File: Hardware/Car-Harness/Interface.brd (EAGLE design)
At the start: 99.6 x 99.8 mm, 56 parts, among them J1 34912-8020, J2 34912-8020, J4 632722110112, J5 OBDII-FEMALEFEMALE, Q1 6.5A/20V/35mΩ, Q2 5.8A/30V/35mΩ, Q3 6.5A/20V/35mΩ, Q4 5.8A/30V/35mΩ

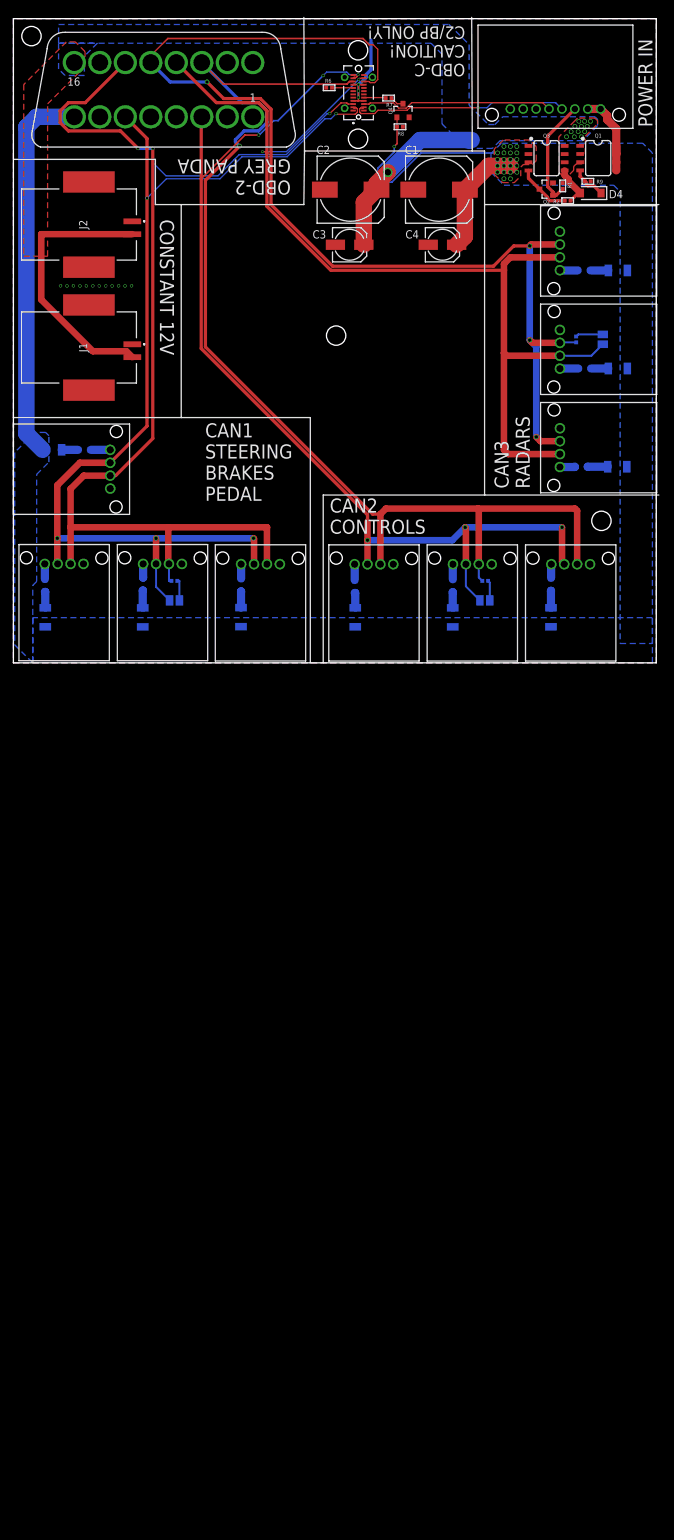
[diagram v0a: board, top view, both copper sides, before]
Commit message: ibooster v2, stm32teensy work
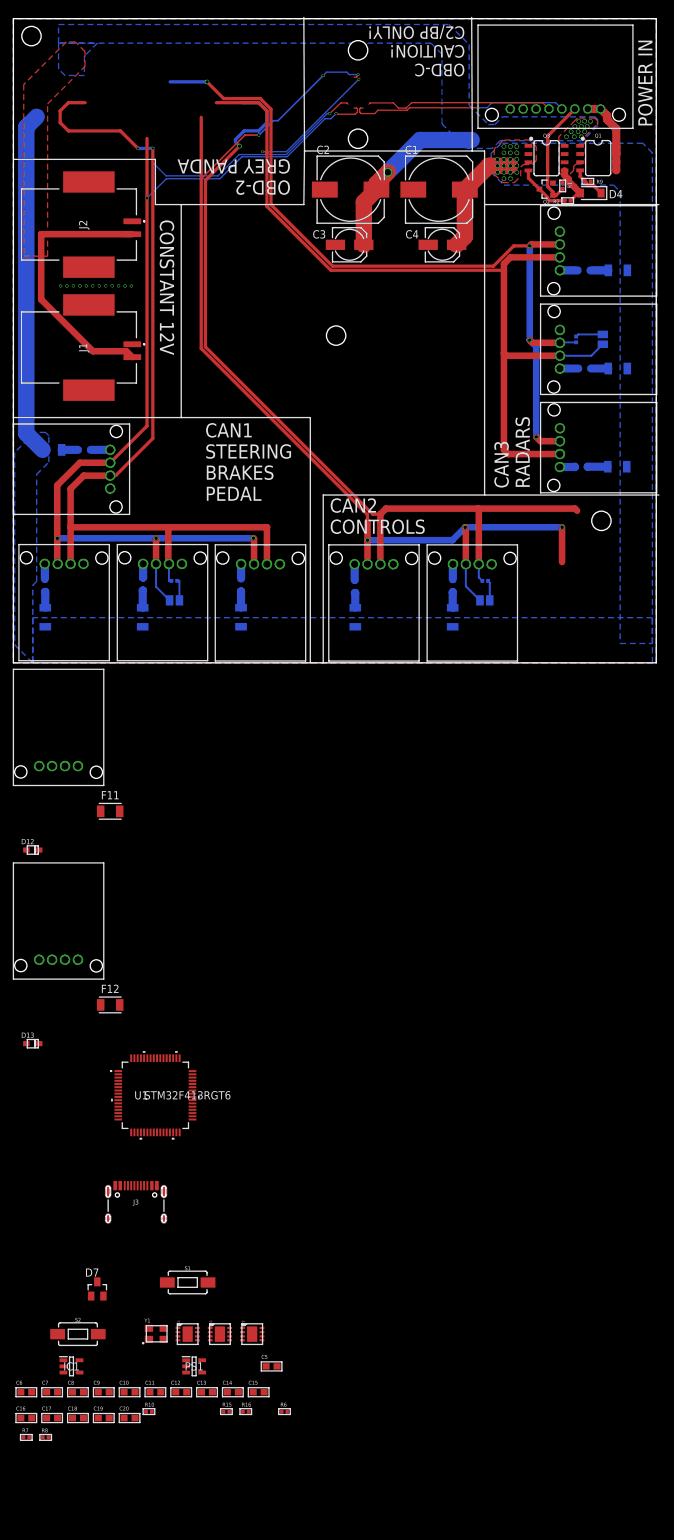
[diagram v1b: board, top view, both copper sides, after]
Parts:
- removed C2-3: MINI50-4, interceptor:MINI50
- removed F6: FUSE_CHIP-1206(3216-METRIC), Circuit-Protection:FUSC3215X82N
- removed J4: 632722110112, SamacSys_Parts:632722110112
- removed J5: OBDII-FEMALEFEMALE, interceptor:OBDII-FEMALE
- removed Q4: 5.8A/30V/35mΩ, SparkFun-DiscreteSemi:SOT23-3
- added C1-5, C1-6: MINI50-4, interceptor:MINI50
- added C10, C11, C12, C13, C14, C15, C16, C17, C18, C9: 100n, comma.ai:0603-C
- added C19, C20: 2.2u, comma.ai:0603-C
- added C5, C6: 22p, comma.ai:0603-C
- added C7, C8: 4.7u, comma.ai:0603-C
- added D12, D13: (no value), adafruit:SOD-323F
- added F11, F12: FUSE_CHIP-1206(3216-METRIC), Circuit-Protection:FUSC3215X82N
- added IC1: MIC5233-3.3YM5-TR, SamacSys_Parts:SOT95P280X145-5N
- added J3: (no value), ROTR-Wireless:USB-C-BREAKOUT_SPARKFUN-CONNECTORS_USB-C-16P
- added PS1: MIC5233-5.0YM5-TR, SamacSys_Parts:SOT95P280X145-5N
- added R10: 5.1k, comma.ai:0402-R
- added R15, R16: 10k, comma.ai:0402-R
- added S1, S2: MOMENTARY-SWITCH-SPST-SMD-6.0X3.5MM, SparkFun-Switches:TACTILE_SWITCH_SMD_6.0X3.5MM
- added U1: STM32F413RGT6, interceptor:LQFP64-10X10MM
- added U2, U3, U4: TJA1042HVSON, comma.ai:HVSON8
- added Y1: CRYSTAL-3.2X2.54-PIN, comma.ai:XTAL-3.2X2.5
- D7: value (none) -> BAS40; device adafruit:SOD-323F -> diode:SOT23
- R6: value 100 -> 22; device interceptor:0402-R -> comma.ai:0402-R
- R7: value 1k -> 22; device interceptor:0402-R -> comma.ai:0402-R
- R8: value 10k -> 5.1k; device interceptor:0402-R -> comma.ai:0402-R
- moved R7 215.0 mm to (2.00, -120.0), turned to 0 degrees
- moved R8 210.3 mm to (5.00, -120.0), turned to 0 degrees
- moved R6 205.2 mm to (42.0, -116.0)
- moved D7 129.8 mm to (13.0, -97.0), flipped to the top, turned to 0 degrees
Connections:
- removed net CAN1H: C1-1.3, C1-2.3, C1-3.3, C1-4.3, J4.A2, J5.6, SJ1.2
- removed net CAN1L: C1-1.2, C1-2.2, C1-3.2, C1-4.2, J4.A3, J5.14, R3.1
- removed net CAN2H: C2-1.3, C2-2.3, C2-3.3, J4.A11, J5.3, SJ2.2
- removed net CAN2L: C2-1.2, C2-2.2, C2-3.2, J4.A10, J5.11, R4.1
- removed net CAN3H: C1-7.3, C1-8.3, C1-9.3, J4.B2, J5.12, SJ3.2
- removed net CAN3L: C1-7.2, C1-8.2, C1-9.2, J4.B3, J5.13, R5.1
- new net 12VIGN1: F11.1
- new net 12VIGN2: F12.1
- new net 3.3V: C10.1, C11.1, C12.1, C14.1, C17.1, C18.1, C20.1, C8.1, C9.1, IC1.5, R16.2, S2.2, U1.13, U1.19, U1.32, U1.48, U1.64, U2.5, U3.5, U4.5
- new net 5V: C13.1, C15.1, C16.1, C19.1, D7.3, IC1.1, IC1.3, PS1.5, U2.3, U3.3, U4.3
- new net CAN1H1: C1-5.3
- new net CAN1H2: C1-6.3
- new net CAN1L1: C1-5.2
- new net CAN1L2: C1-6.2
- new net CAN1_EN: U1.9, U2.8
- new net CAN1_H: C1-1.3, C1-2.3, C1-3.3, C1-4.3, SJ1.2, U2.7
- new net CAN1_L: C1-1.2, C1-2.2, C1-3.2, C1-4.2, R3.1, U2.6
- new net CAN1_RX: U1.61, U2.4
- new net CAN1_TX: U1.62, U2.1
- new net CAN2_EN: U1.2, U3.8
- new net CAN2_H: C2-1.3, C2-2.3, SJ2.2, U3.7
- new net CAN2_L: C2-1.2, C2-2.2, R4.1, U3.6
- new net CAN2_RX: U1.57, U3.4
- new net CAN2_TX: U1.58, U3.1
- new net CAN3_EN: U1.14, U4.8
- new net CAN3_H: C1-7.3, C1-8.3, C1-9.3, SJ3.2, U4.7
- new net CAN3_L: C1-7.2, C1-8.2, C1-9.2, R5.1, U4.6
- new net CAN3_RX: U1.41, U4.4
- new net CAN3_TX: U1.50, U4.1
- new net N$31: C1-6.4, D13.C
- new net N$32: R6.2, U1.45
- new net N$33: J3.A5, R10.2
- new net N$34: J3.B5, R8.2
- new net N$35: J3.A6, J3.B6, R6.1
- new net N$36: J3.A7, J3.B7, R7.1
- new net N$37: D7.1, J3.VBUS1, J3.VBUS2
- new net N$38: R16.1, S1.1, U1.7
- new net N$39: R15.2, S2.1, U1.60
- new net N$40: C7.1, U1.30
- new net N$43: C6.1, U1.6, Y1.1
- new net PWRON: U1.33
- new net VBAT: U1.1
- net 12V: now also PS1.1, PS1.3; no longer J4.A4, J4.A9, J4.B4, J4.B9, J5.16
- net 12VIGN: no longer F6.1, J5.8, Q4.1, R8.2
- net CAN4H: no longer J4.B11
- net CAN4L: no longer J4.B10
- net GND: now also C1-5.1, C1-6.1, C10.2, C11.2, C12.2, C13.2, C14.2, C15.2, C16.2, C17.2, C18.2, C19.2, C20.2, C5.2, C6.2, C7.2, C8.2, C9.2, IC1.2, J3.GND, J3.GND2, J3.SHLD1, J3.SHLD2, J3.SHLD3, J3.SHLD4, J3.SHLD5, J3.SHLD6, J3.SHLD7, J3.SHLD8, PS1.2, R10.1, R15.1, S1.2, U1.12, U1.18, U1.31, U1.47, U1.63, U2.2, U2.PAD, U3.2, U3.PAD, U4.2, U4.PAD; no longer C2-3.1, J4.A1, J4.A12, J4.B1, J4.B12, J4.MH3, J4.MH4, J4.MH5, J4.MH6, J5.4, J5.5, Q4.2, R6.1
- net N$14: now also C5.1, U1.5, Y1.3; no longer D7.A, F6.2
- net N$16: now also R7.2, U1.44; no longer C2-3.4, D7.C
- net N$25: now also D12.A, F11.2; no longer J4.B8, R7.2
- net N$29: now also C1-5.4, D12.C; no longer Q4.3, R7.1
- net N$30: now also D13.A, F12.2; no longer J4.A8, R6.2
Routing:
- net CAN1L: track 187.2 -> 0.00 mm, vias 3 -> 0
- net CAN1_L: track 0.00 -> 177.7 mm, vias 0 -> 3
- net CAN2L: track 176.9 -> 0.00 mm, vias 1 -> 0
- net CAN3L: track 173.0 -> 0.00 mm, vias 4 -> 0
- net CAN1H: track 163.6 -> 0.00 mm, vias 5 -> 0
- net CAN2H: track 161.5 -> 0.00 mm, vias 6 -> 0
- net CAN2_H: track 0.00 -> 160.7 mm, vias 0 -> 6
- net CAN1_H: track 0.00 -> 158.6 mm, vias 0 -> 5
- net CAN3H: track 157.0 -> 0.00 mm, vias 2 -> 0
- net CAN3_H: track 0.00 -> 147.6 mm, vias 0 -> 2
- net CAN2_L: track 0.00 -> 134.8 mm, vias 0 -> 1
- net CAN3_L: track 0.00 -> 123.6 mm, vias 0 -> 4
- net 12VIGN: track 108.0 -> 71.0 mm, vias 22 -> 20
- net 12V: track 92.1 -> 76.4 mm, vias 16 -> 13
- net N$25: track 3.41 -> 0.00 mm
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
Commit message: ibooster gateway
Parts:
- removed D7: BAS40, diode:SOT23
- removed R10, R8: 5.1k, comma.ai:0402-R
- added U$2: TPS25830, packages(ti):RHB.32
- moved J3 49.0 mm to (5.00, -128.0)
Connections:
- removed net CAN4H: U$1.P$4
- removed net CAN4L: U$1.P$5
- new net N$41: J3.A7, J3.B7, U$2.17
- new net N$42: J3.VBUS1, J3.VBUS2, U$2.15
- new net N$44: J3.GND, J3.GND2, J3.SHLD1, J3.SHLD2, J3.SHLD3, J3.SHLD4, J3.SHLD5, J3.SHLD6, J3.SHLD7, J3.SHLD8
- net 5V: no longer D7.3
- net GND: now also U$1.P$6; no longer J3.GND, J3.GND2, J3.SHLD1, J3.SHLD2, J3.SHLD3, J3.SHLD4, J3.SHLD5, J3.SHLD6, J3.SHLD7, J3.SHLD8, R10.1, R8.1
- net N$10: now also U$1.P$3
- net N$12: now also U$1.P$5; no longer U$1.P$3
- net N$33: now also U$2.20; no longer R10.2
- net N$34: now also U$2.19; no longer R8.2
- net N$35: no longer J3.A6, J3.B6
- net N$36: no longer J3.A7, J3.B7
- net N$37: now also J3.A6, J3.B6, U$2.18; no longer D7.1, J3.VBUS1, J3.VBUS2
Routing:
- net CAN4H: track 33.6 -> 0.00 mm, vias 1 -> 0
- net CAN4L: track 29.0 -> 0.00 mm
- net N$12: track 17.4 -> 11.4 mm
